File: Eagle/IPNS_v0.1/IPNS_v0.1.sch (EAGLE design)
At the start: 27 parts, among them Q1 16MHz, Q2 32.768 kHz, U1 STM8L152C4_C6TX

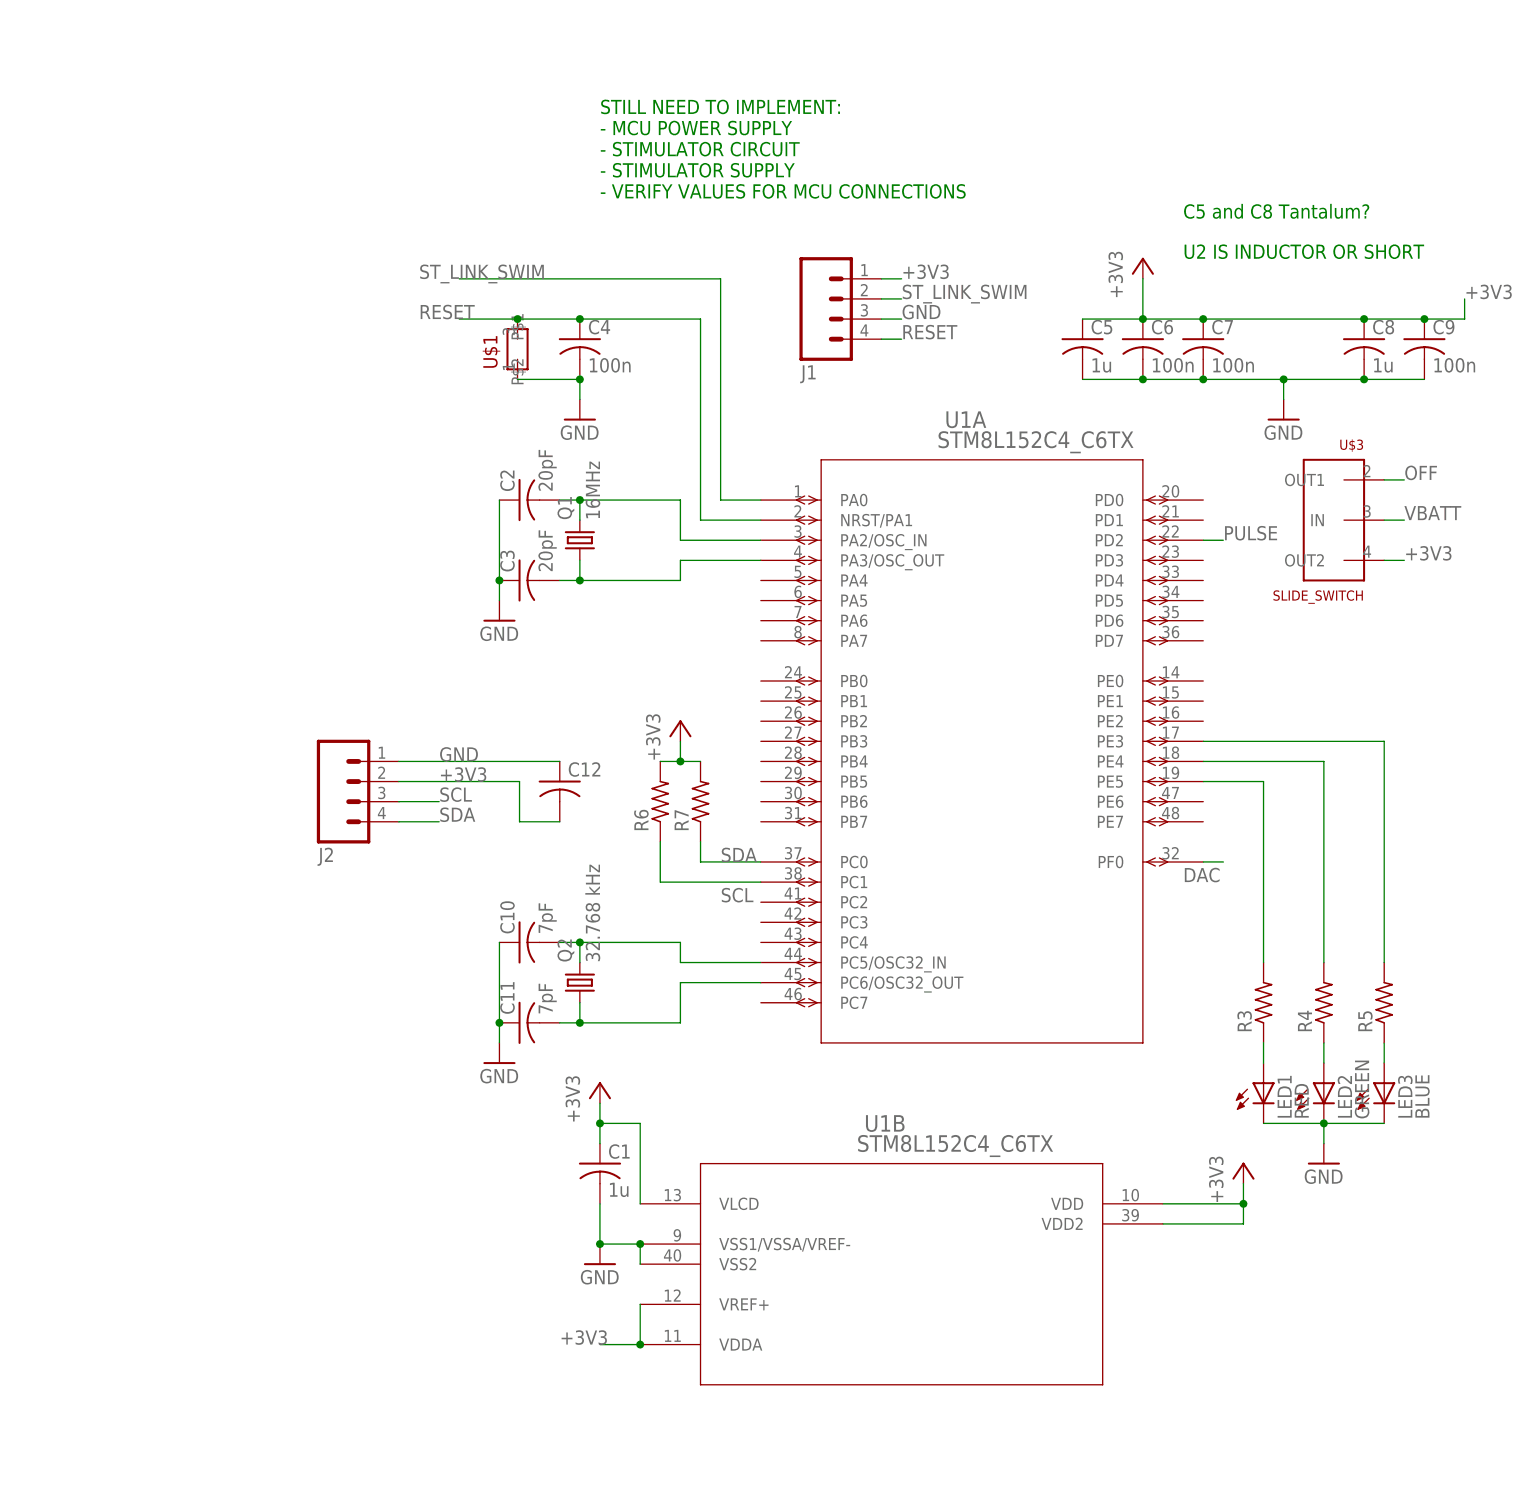
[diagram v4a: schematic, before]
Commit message: All connections wired except for STM8L breakout pins
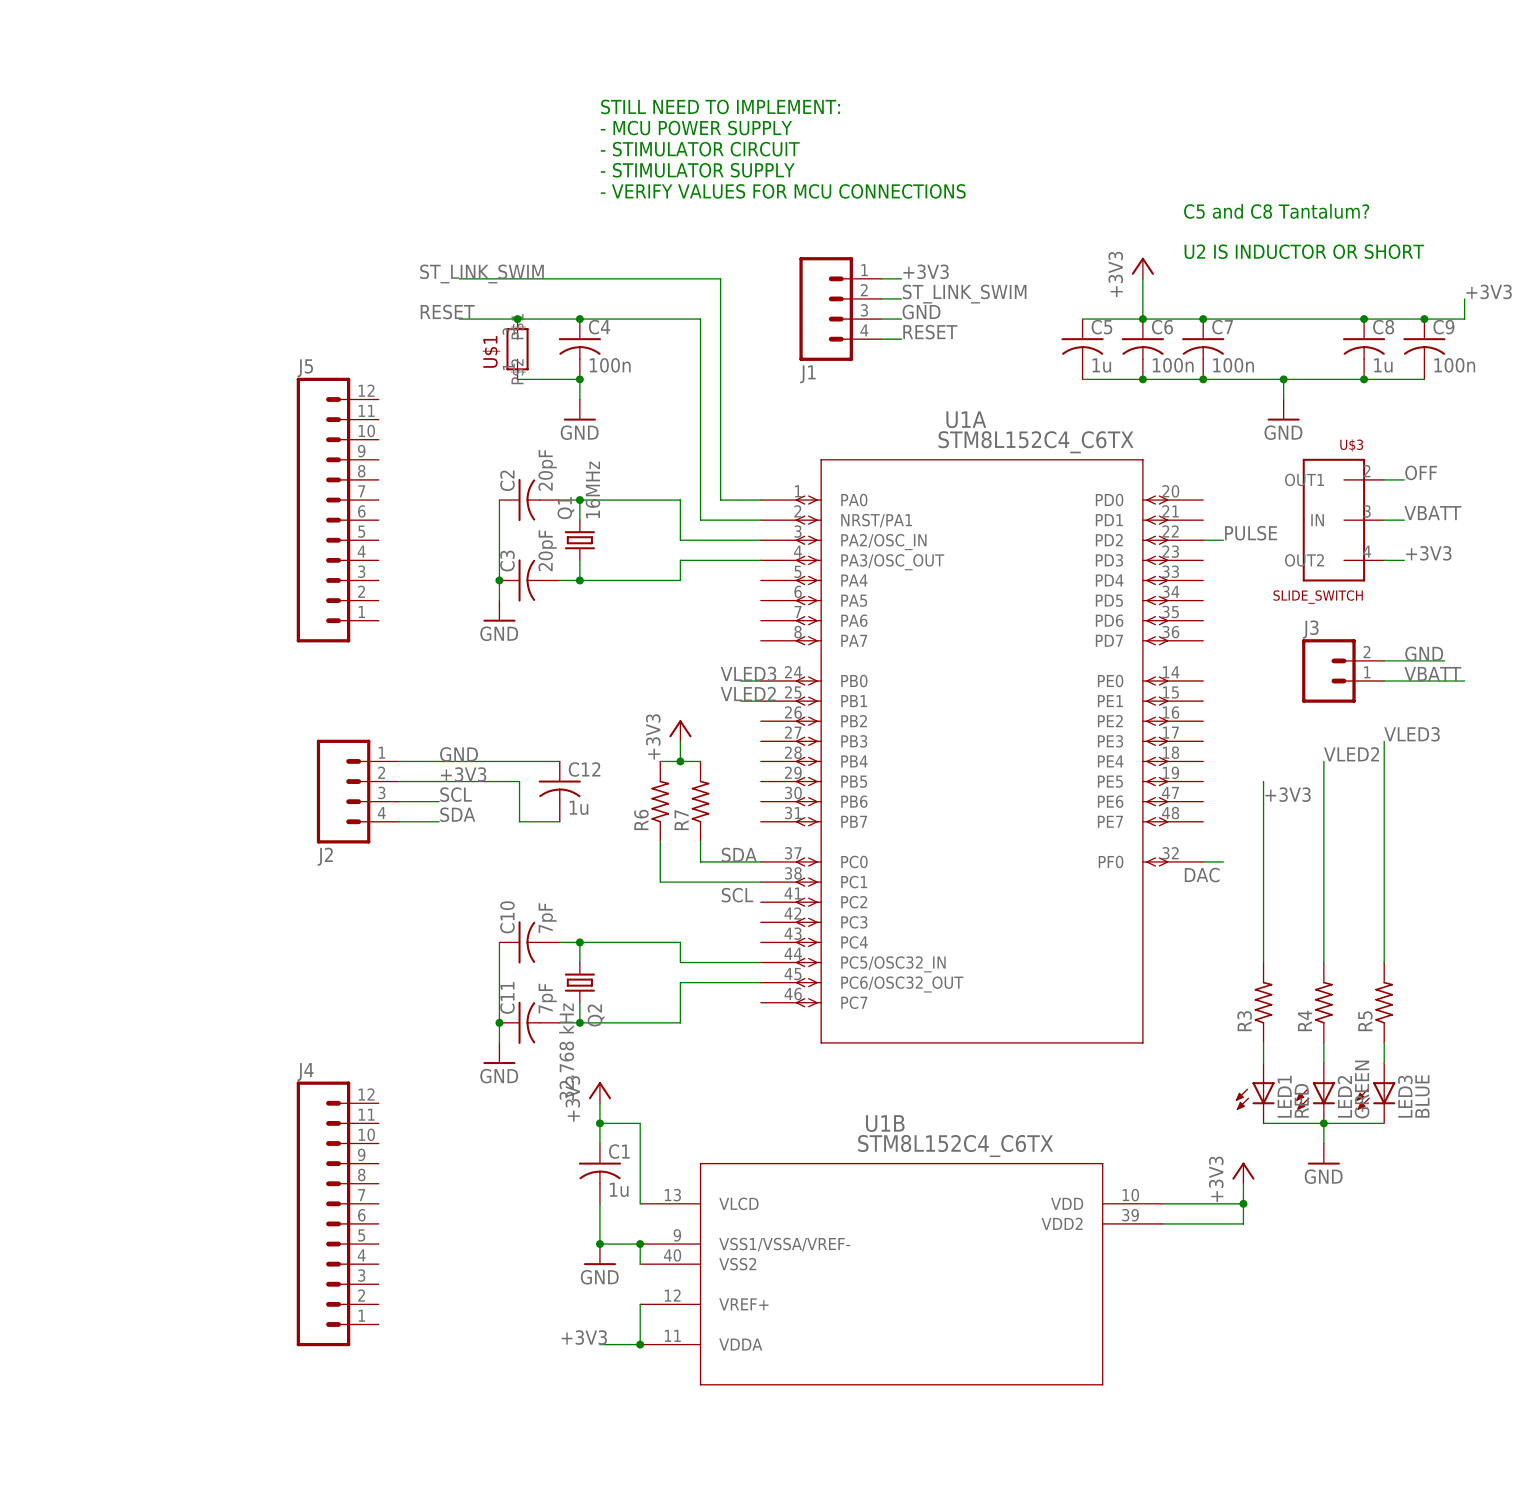
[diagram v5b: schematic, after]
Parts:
- added J3: (no value), IPNS_Lib_v0.1:M02PTH
- added J4, J5: (no value), IPNS_Lib_v0.1:M12PTH
- C12: value (none) -> 1u
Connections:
- removed net N$14: R3.2, U1A.PE5
- removed net N$15: R4.2, U1A.PE4
- removed net N$16: R5.2, U1A.PE3
- new net VLED2: R4.2, U1A.PB1
- new net VLED3: R5.2, U1A.PB0
- net +3V3: now also R3.2
- net GND: now also J3.2
- net N$3: now also Q2.2; no longer Q2.1
- net N$6: now also Q2.1; no longer Q2.2
- net VBATT: now also J3.1
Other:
- moved on the sheet: Q2
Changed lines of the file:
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@@
 </variantdefs>
 <classes>
-<class number="0" name="default" width="0" drill="0">
+<class number="0" name="default" width="0.1778" drill="0.254">
+<clearance class="0" value="0.2032"/>
 </class>
 </classes>
@@
 <part name="GND6" library="IPNS_Lib_v0.1" deviceset="GND" device=""/>
 <part name="J2" library="IPNS_Lib_v0.1" deviceset="M04" device="PTH"/>
-<part name="C12" library="IPNS_Lib_v0.1" deviceset="C-US" device="C0805"/>
+<part name="C12" library="IPNS_Lib_v0.1" deviceset="C-US" device="C0805" value="1u"/>
 <part name="R6" library="IPNS_Lib_v0.1" deviceset="R-US_" device="R0805"/>
 <part name="R7" library="IPNS_Lib_v0.1" deviceset="R-US_" device="R0805"/>
 <part name="+3V4" library="IPNS_Lib_v0.1" deviceset="+3V3" device=""/>
 <part name="U$3" library="IPNS_Lib_v0.1" deviceset="SLIDE_SWITCH" device=""/>
+<part name="J3" library="IPNS_Lib_v0.1" deviceset="M02" device="PTH"/>
+<part name="J4" library="IPNS_Lib_v0.1" deviceset="M12" device="PTH"/>
+<part name="J5" library="IPNS_Lib_v0.1" deviceset="M12" device="PTH"/>
 </parts>
 <sheets>
@@
 <instance part="GND4" gate="1" x="78.74" y="104.14"/>
 <instance part="+3V3" gate="G$1" x="60.96" y="124.46"/>
-<instance part="Q2" gate="G$1" x="-10.16" y="33.02" rot="R90"/>
+<instance part="Q2" gate="G$1" x="-10.16" y="33.02" rot="R270"/>
 <instance part="C10" gate="G$1" x="-17.78" y="38.1" rot="R90"/>
 <instance part="C11" gate="G$1" x="-17.78" y="27.94" rot="R90"/>
@@
 <instance part="+3V4" gate="G$1" x="2.54" y="66.04"/>
 <instance part="U$3" gate="G$1" x="83.82" y="91.44" rot="MR0"/>
+<instance part="J3" gate="G$1" x="83.82" y="71.12"/>
+<instance part="J4" gate="G$1" x="-45.72" y="5.08"/>
+<instance part="J5" gate="G$1" x="-45.72" y="93.98"/>
 </instances>
 <busses>
@@
 <label x="-12.7" y="-12.7" size="1.778" layer="95"/>
 </segment>
+<segment>
+<pinref part="R3" gate="G$1" pin="2"/>
+<wire x1="76.2" y1="35.56" x2="76.2" y2="58.42" width="0.1524" layer="91"/>
+<label x="76.2" y="55.88" size="1.778" layer="95"/>
+</segment>
 </net>
 <net name="GND" class="0">
@@
 <wire x1="-33.02" y1="60.96" x2="-12.7" y2="60.96" width="0.1524" layer="91"/>
 </segment>
+<segment>
+<pinref part="J3" gate="G$1" pin="2"/>
+<wire x1="91.44" y1="73.66" x2="99.06" y2="73.66" width="0.1524" layer="91"/>
+<label x="93.98" y="73.66" size="1.778" layer="95"/>
+</segment>
 </net>
 <net name="N$1" class="0">
@@
 <segment>
 <pinref part="C11" gate="G$1" pin="2"/>
-<pinref part="Q2" gate="G$1" pin="1"/>
-<wire x1="-10.16" y1="27.94" x2="-12.7" y2="27.94" width="0.1524" layer="91"/>
-<wire x1="-10.16" y1="30.48" x2="-10.16" y2="27.94" width="0.1524" layer="91"/>
-<junction x="-10.16" y="27.94"/>
 <pinref part="U1" gate="A" pin="PC6/OSC32_OUT"/>
 <wire x1="12.7" y1="33.02" x2="2.54" y2="33.02" width="0.1524" layer="91"/>
 <wire x1="2.54" y1="33.02" x2="2.54" y2="27.94" width="0.1524" layer="91"/>
+<wire x1="-12.7" y1="27.94" x2="-10.16" y2="27.94" width="0.1524" layer="91"/>
+<pinref part="Q2" gate="G$1" pin="2"/>
 <wire x1="-10.16" y1="27.94" x2="2.54" y2="27.94" width="0.1524" layer="91"/>
+<wire x1="-10.16" y1="30.48" x2="-10.16" y2="27.94" width="0.1524" layer="91"/>
+<junction x="-10.16" y="27.94"/>
 </segment>
 </net>
 <net name="N$6" class="0">
 <segment>
-<pinref part="Q2" gate="G$1" pin="2"/>
-<wire x1="-10.16" y1="35.56" x2="-10.16" y2="38.1" width="0.1524" layer="91"/>
 <pinref part="C10" gate="G$1" pin="2"/>
-<wire x1="-10.16" y1="38.1" x2="-12.7" y2="38.1" width="0.1524" layer="91"/>
 <pinref part="U1" gate="A" pin="PC5/OSC32_IN"/>
 <wire x1="12.7" y1="35.56" x2="2.54" y2="35.56" width="0.1524" layer="91"/>
 <wire x1="2.54" y1="35.56" x2="2.54" y2="38.1" width="0.1524" layer="91"/>
 <wire x1="2.54" y1="38.1" x2="-10.16" y2="38.1" width="0.1524" layer="91"/>
+<pinref part="Q2" gate="G$1" pin="1"/>
+<wire x1="-10.16" y1="38.1" x2="-12.7" y2="38.1" width="0.1524" layer="91"/>
+<wire x1="-10.16" y1="35.56" x2="-10.16" y2="38.1" width="0.1524" layer="91"/>
 <junction x="-10.16" y="38.1"/>
 </segment>
@@
 </segment>
 </net>
-<net name="N$14" class="0">
-<segment>
-<pinref part="R3" gate="G$1" pin="2"/>
-<wire x1="76.2" y1="35.56" x2="76.2" y2="58.42" width="0.1524" layer="91"/>
-<pinref part="U1" gate="A" pin="PE5"/>
-<wire x1="76.2" y1="58.42" x2="68.58" y2="58.42" width="0.1524" layer="91"/>
-</segment>
-</net>
-<net name="N$15" class="0">
+<net name="VLED2" class="0">
 <segment>
 <pinref part="R4" gate="G$1" pin="2"/>
 <wire x1="83.82" y1="35.56" x2="83.82" y2="60.96" width="0.1524" layer="91"/>
-<pinref part="U1" gate="A" pin="PE4"/>
-<wire x1="83.82" y1="60.96" x2="68.58" y2="60.96" width="0.1524" layer="91"/>
-</segment>
-</net>
-<net name="N$16" class="0">
+<label x="83.82" y="60.96" size="1.778" layer="95"/>
+</segment>
+<segment>
+<pinref part="U1" gate="A" pin="PB1"/>
+<wire x1="12.7" y1="68.58" x2="10.16" y2="68.58" width="0.1524" layer="91"/>
+<label x="7.62" y="68.58" size="1.778" layer="95"/>
+</segment>
+</net>
+<net name="VLED3" class="0">
 <segment>
 <pinref part="R5" gate="G$1" pin="2"/>
 <wire x1="91.44" y1="35.56" x2="91.44" y2="63.5" width="0.1524" layer="91"/>
-<pinref part="U1" gate="A" pin="PE3"/>
-<wire x1="91.44" y1="63.5" x2="68.58" y2="63.5" width="0.1524" layer="91"/>
+<label x="91.44" y="63.5" size="1.778" layer="95"/>
+</segment>
+<segment>
+<pinref part="U1" gate="A" pin="PB0"/>
+<wire x1="12.7" y1="71.12" x2="10.16" y2="71.12" width="0.1524" layer="91"/>
+<label x="7.62" y="71.12" size="1.778" layer="95"/>
 </segment>
 </net>
@@
 <label x="93.98" y="91.44" size="1.778" layer="95"/>
 </segment>
-</net>
+<segment>
+<pinref part="J3" gate="G$1" pin="1"/>
+<wire x1="91.44" y1="71.12" x2="101.6" y2="71.12" width="0.1524" layer="91"/>
+<label x="93.98" y="71.12" size="1.778" layer="95"/>
+</segment>
+</net>
